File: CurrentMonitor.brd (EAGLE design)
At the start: 80 x 100 mm, 68 parts, among them IC1 MEGA8-AI, IC2 INA138, IC3 INA138, IC4 LF33CV, J1 AVR_SPI_PRG_6OFFSET_PADS, Q1 10MHz, Q2 IRLZ34N, Q3 IRLZ34N, Q4 IRLZ34N, Q6 BC847, Q7 IRF9530, Q8 IRF9530, Q9 BC847, X1 MSTBV2, X2 MSTBV2, X3 MSTBV2, X5 MSTBV2

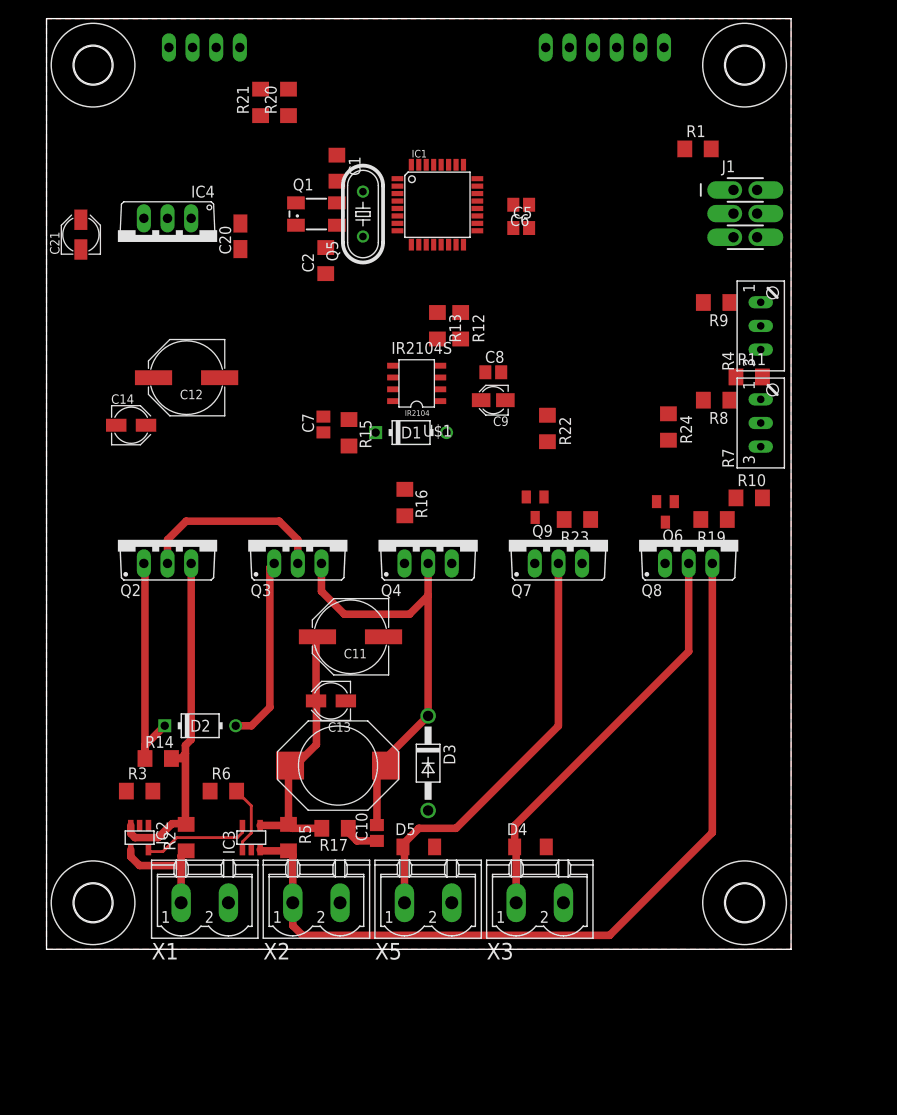
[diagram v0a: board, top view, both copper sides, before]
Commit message: Added initial board. WARNING: This is an ugly board, which didn't receive much love because it's a prototype and I can't etch double-sided boards yet.
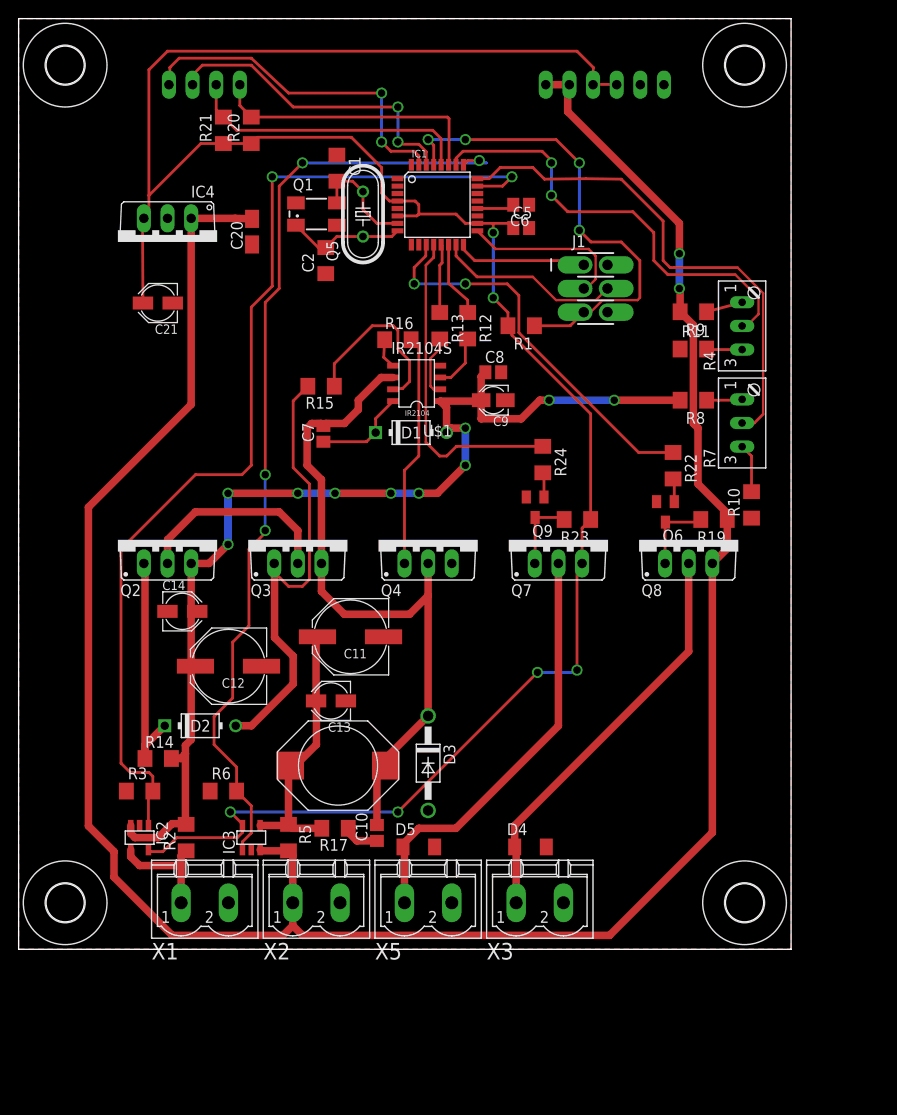
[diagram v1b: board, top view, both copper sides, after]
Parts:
- moved C12 31.3 mm to (19.6, 30.4)
- moved R1 26.9 mm to (51.0, 67.0), turned to 180 degrees
- moved C14 20.7 mm to (14.6, 36.3)
- moved J1 18.0 mm to (59.0, 71.0)
- moved R16 17.5 mm to (37.8, 65.5), turned to 0 degrees
- moved R22 14.1 mm to (67.3, 52.0)
- moved R24 13.9 mm to (53.3, 52.6)
- moved C21 11.1 mm to (12.0, 69.4), turned to 180 degrees
- moved R11 6.71 mm to (69.5, 64.5)
- moved R15 5.83 mm to (29.5, 60.5), turned to 180 degrees
- moved R20 5.00 mm to (22.0, 88.0)
- moved R21 5.00 mm to (19.0, 88.0)
- moved JP1 4.00 mm to (60.0, 92.9)
- moved JP2 4.00 mm to (17.0, 92.9)
- moved U$2 3.00 mm to (2.00, 5.00)
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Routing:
- net +3V3: track 11.8 -> 239.7 mm, vias 0 -> 6
- net BAT+: track 90.3 -> 257.4 mm, vias 0 -> 2
- net ADC0: track 0.00 -> 112.0 mm, vias 0 -> 2
- net ADC2: track 7.35 -> 102.2 mm, vias 0 -> 4
- net CELL_TO_CONTROLLER: track 37.6 -> 117.7 mm, vias 0 -> 10
- net ADC1: track 0.00 -> 54.9 mm
- net RESET: track 0.00 -> 51.9 mm, vias 0 -> 4
- net ADC3: track 0.00 -> 48.0 mm, vias 0 -> 2
- net EN_CIRCUIT: track 0.00 -> 42.4 mm, vias 0 -> 2
- net TXD: track 0.00 -> 37.4 mm, vias 0 -> 2
- net EN_3V3: track 0.00 -> 35.2 mm
- net RXD: track 0.00 -> 34.0 mm, vias 0 -> 2
- net SCL: track 0.00 -> 31.0 mm
- net SDA: track 0.00 -> 30.3 mm
- net N$13: track 20.2 -> 49.6 mm
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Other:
- board size 80 x 100 mm -> 83 x 100 mm

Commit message: Second revision, dual layer
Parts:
- moved R9 53.4 mm to (59.8, 16.0)
- moved R4 51.8 mm to (66.8, 16.0), flipped to the bottom, turned to 270 degrees
- moved R20 43.8 mm to (9.50, 46.0)
- moved R11 43.8 mm to (64.8, 21.0)
- moved R21 42.6 mm to (12.0, 46.0)
- moved C20 42.6 mm to (11.0, 36.0), turned to 180 degrees
- moved R22 41.0 mm to (48.9, 15.3), turned to 0 degrees
- moved IC4 38.8 mm to (5.37, 38.0), flipped to the bottom
- moved U$5 38.6 mm to (65.2, 57.6)
- moved U$3 37.5 mm to (5.17, 57.6)
- moved JP1 36.5 mm to (49.8, 57.9), turned to 180 degrees
- moved R8 36.3 mm to (60.0, 24.0)
- moved C1 35.7 mm to (22.7, 49.3), turned to 0 degrees
- moved U$1 35.1 mm to (45.1, 27.7)
- moved JP2 35.0 mm to (16.8, 57.9)
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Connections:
- net MPPT_ENABLE: now also IC1.13; no longer IC1.14
- net MPPT_PWM: now also IC1.14; no longer IC1.13
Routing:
- net +3V3: track 239.7 -> 169.7 mm, vias 6 -> 2
- net BAT+: track 257.4 -> 212.5 mm, vias 2 -> 0
- net ADC0: track 112.0 -> 70.9 mm
- net N$13: track 49.6 -> 18.8 mm
- net ADC2: track 102.2 -> 72.2 mm, vias 4 -> 2
- net ADC3: track 48.0 -> 75.5 mm, vias 2 -> 3
- net VS: track 74.3 -> 47.8 mm, vias 0 -> 1
- net N$20: track 8.37 -> 30.9 mm
- net RESET: track 51.9 -> 30.2 mm, vias 4 -> 2
- net SDA: track 30.3 -> 46.7 mm
- net N$11: track 25.1 -> 8.95 mm
- net SCL: track 31.0 -> 47.1 mm
- net CELL_TO_CONTROLLER: track 117.7 -> 102.4 mm, vias 10 -> 1
- net MPPT_PWM: track 7.43 -> 21.3 mm
- net N$12: track 25.4 -> 12.8 mm
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- added copper zone on layer 16, net GND
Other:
- board size 83 x 100 mm -> 70 x 62.6 mm

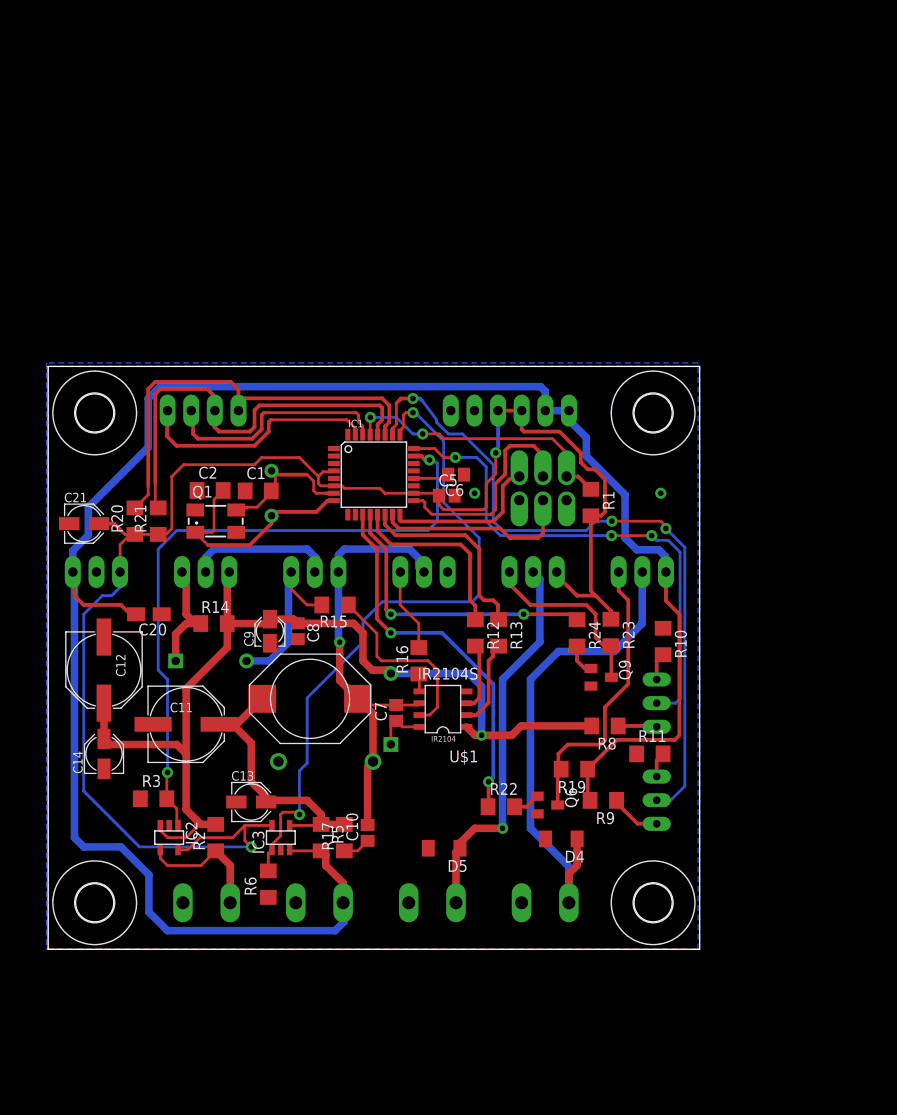
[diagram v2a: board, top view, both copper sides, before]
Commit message: Added slightly larger traces and adjusted some components in order to support currents up to 10A
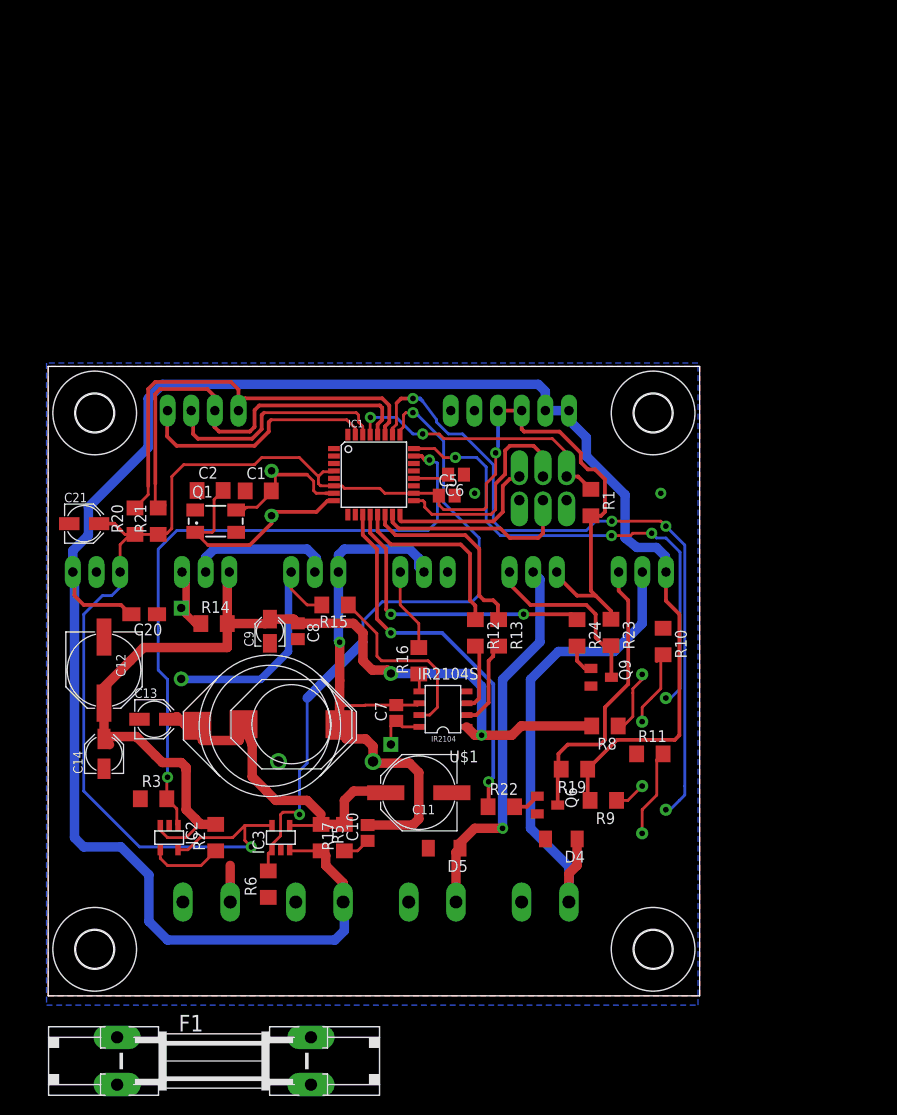
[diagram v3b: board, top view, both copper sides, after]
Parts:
- added F1: (no value), fuse:SHKOG
- added L2: 10µ, Inductor-Fastron:PISR
- R4, R7: device pot:S64W -> rcl:RTRIM64P
- X1, X2, X3, X5: value MSTBV2 -> MSTBA2; device con-phoenix-508:MSTBV2 -> con-phoenix-508:MSTBA2
- moved C11 26.1 mm to (40.0, 16.8), turned to 180 degrees
- moved C13 13.7 mm to (11.6, 24.7)
- moved U$2 5.00 mm to (5.17, 0.00)
- moved U$4 5.00 mm to (65.2, 0.00)
- moved X1 5.00 mm to (17.2, 0.00)
- moved X2 5.00 mm to (29.3, 0.00)
- moved X3 5.00 mm to (53.6, 0.00)
- moved X5 5.00 mm to (41.5, 0.00)
- moved D2 3.72 mm to (14.5, 32.9), turned to 270 degrees
- moved L1 3.38 mm to (26.3, 24.2)
- moved R4 3.01 mm to (64.0, 15.0), turned to 180 degrees
- moved R7 2.89 mm to (64.0, 27.0), turned to 180 degrees
- moved C20 0.51 mm to (10.5, 36.0)
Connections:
- new net N$123: F1.2A, IC2.4, R2.1
- net ADC1: now also R7.2; no longer R7.S
- net ADC3: now also R4.2; no longer R4.S
- net CONTROLLER_TO_BAT: now also L2.1
- net FROM_CELL: now also F1.1A; no longer IC2.4, R2.1
- net N$2: now also R4.3; no longer R4.E
- net N$3: now also R7.3; no longer R7.E
- net N$4: now also R7.1; no longer R7.A
- net N$5: now also R4.1; no longer R4.A
- net VS: now also L2.2
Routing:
- net VS: track 47.8 -> 62.9 mm
- net CONTROLLER_TO_BAT: track 29.2 -> 40.4 mm
- net FROM_CELL: track 14.1 -> 3.94 mm
- net N$13: track 18.8 -> 27.3 mm
- net N$123: track 0.00 -> 7.84 mm
- net N$2: track 2.72 -> 9.47 mm
- net N$3: track 2.95 -> 9.09 mm
- net N$12: track 12.8 -> 7.61 mm
- net CELL_TO_CONTROLLER: track 102.4 -> 106.3 mm
- net N$4: track 4.18 -> 6.95 mm
- net N$5: track 5.51 -> 3.64 mm
- net BAT+: track 212.5 -> 214.2 mm
- net ADC1: track 55.1 -> 53.5 mm
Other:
- board size 70 x 62.6 mm -> 70 x 67.6 mm

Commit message: Added heatsink + LEDs
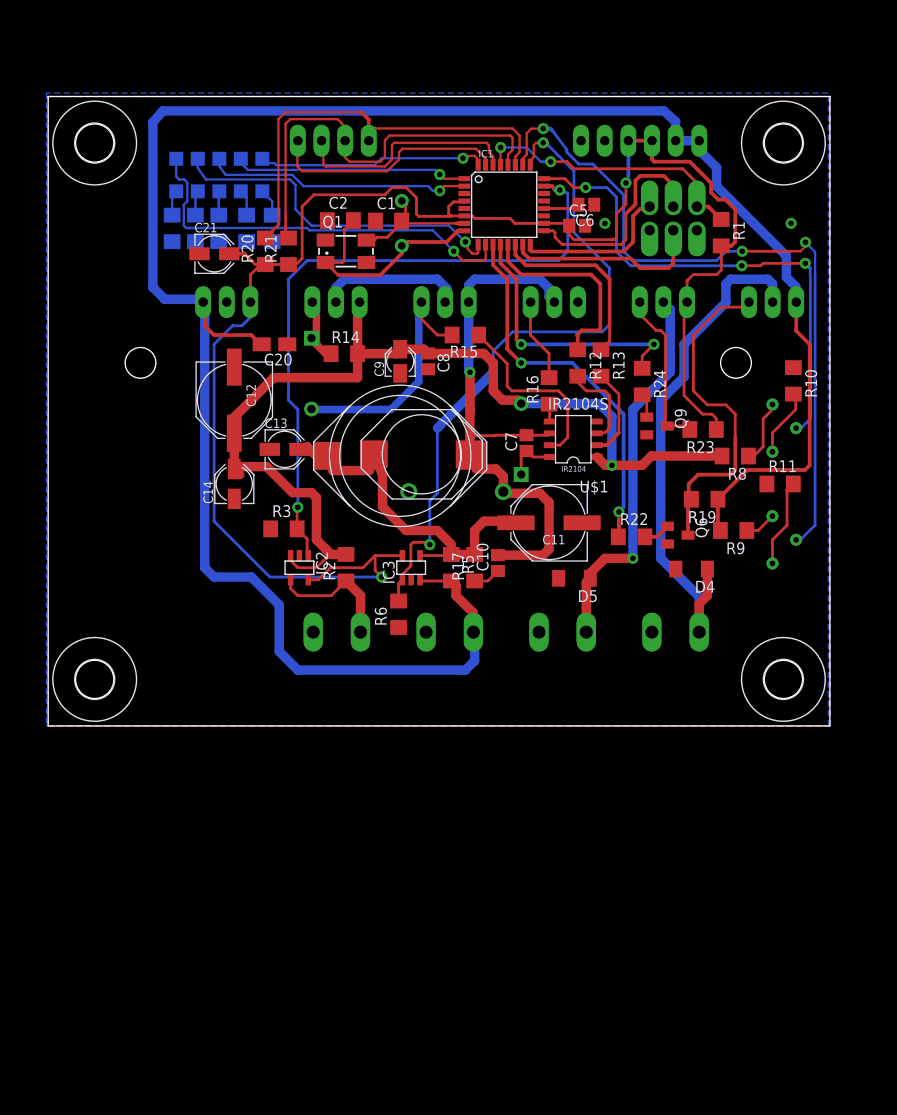
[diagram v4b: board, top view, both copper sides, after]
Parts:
- removed F1: (no value), fuse:SHKOG
- added LED1, LED2, LED3, LED4, LED5: (no value), led:CHIPLED_1206
- added R18, R25, R26, R27, R28: (no value), rcl:R1206
- added U$6: (no value), heatsink:SK125/84
- R1, R10, R11, R12, R13, R19, R20, R21, R22, R23, R24, R3, R6, R8, R9: device rcl:R1206@1 -> rcl:R1206
- moved C1 32.2 mm to (36.7, 78.3)
- moved Q3 32.2 mm to (42.8, 67.0)
- moved R1 32.2 mm to (72.5, 77.0)
- moved R6 32.2 mm to (37.8, 36.0)
- moved X2 32.2 mm to (43.3, 29.0)
- moved C10 32.2 mm to (48.5, 41.5)
- moved C11 32.2 mm to (54.0, 45.8)
- moved C12 32.2 mm to (20.2, 59.0)
- moved C13 32.2 mm to (25.6, 53.7)
- moved C14 32.2 mm to (20.2, 50.0)
- moved C2 32.2 mm to (31.6, 78.3)
- moved C20 32.2 mm to (24.5, 65.0)
- moved C21 32.2 mm to (18.0, 74.7)
- moved C5 32.2 mm to (57.0, 77.7)
- moved C6 32.2 mm to (58.0, 80.0)
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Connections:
- removed net N$123: F1.2A, IC2.4, R2.1
- removed net N$15: IC1.10
- removed net N$16 (its old number): IC1.9
- removed net N$19: IC1.1
- new net LED1: IC1.32, LED1.A
- new net LED2: IC1.1, LED2.A
- new net LED3: IC1.2, LED3.A
- new net LED4: IC1.9, LED4.A
- new net LED5: IC1.10, LED5.A
- new net N$26: LED3.C, R26.1
- new net N$29: LED4.C, R27.1
- new net N$32: LED5.C, R28.1
- new net N$6: LED1.C, R18.1
- net FROM_CELL: now also IC2.4, R2.1; no longer F1.1A
- net GND: now also R18.2, R25.2, R26.2, R27.2, R28.2
- net N$18: now also LED2.C, R25.1; no longer IC1.2
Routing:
- net LED5: track 0.00 -> 43.7 mm, vias 0 -> 1
- net LED4: track 0.00 -> 37.8 mm, vias 0 -> 1
- net LED3: track 0.00 -> 28.5 mm, vias 0 -> 1
- net LED2: track 0.00 -> 25.8 mm, vias 0 -> 1
- net LED1: track 0.00 -> 24.6 mm, vias 0 -> 1
- net BAT+: track 214.2 -> 228.2 mm
- net FROM_CELL: track 3.94 -> 14.0 mm
- net +3V3: track 169.7 -> 179.1 mm
- net N$123: track 7.84 -> 0.00 mm
- net N$20: track 30.9 -> 36.4 mm
- net N$16: track 52.8 -> 56.6 mm
- net N$6: track 0.00 -> 3.00 mm
- net EN_3V3: track 31.9 -> 29.0 mm
- net N$18: track 0.00 -> 2.82 mm
- net N$32: track 0.00 -> 2.74 mm
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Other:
- board size 70 x 67.6 mm -> 84 x 67.6 mm

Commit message: Foo (don't know what's changed, but I'm going to reroute everything)
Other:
- board text added: "MoarChargezzzzzz Rev. A"
- board text added: "Top"
